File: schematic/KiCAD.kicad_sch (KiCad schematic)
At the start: 7 parts, among them J1 Raspberry_Pi_4, U1 NUCLEO-F401RE, U2 ACS712xLCTR-05B, U3 ACS712xLCTR-05B, U4 ACS712xLCTR-05B, U5 L298N

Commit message: new schematic
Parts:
- removed U6: (no value), Package_DFN_QFN:WDFN-10-1EP_3x3mm_P0.5mm_EP1.8x2.5mm, symbol Lab2_Modules:HW688_Buck
- added Buck-converter: (no value), symbol Lab2_Modules:HW688_Buck
- added Left-Rear-Motor, Right-Rear-Motor: (no value), symbol Lab2_Modules:Motor_With_Encoder
- added Servo: (no value), symbol Lab2_Modules:Servo
- U2: value ACS712xLCTR-05B -> Left Rear Motor Current sensor
- U3: value ACS712xLCTR-05B -> Right Rear Motor Current sensor
- U4: value ACS712xLCTR-05B -> Servo Current Sensor
- U5: value L298N -> H bridge
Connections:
- new net GND_S2: U1.10_20 (GND_S2), U1.10_9 (GND_S2)

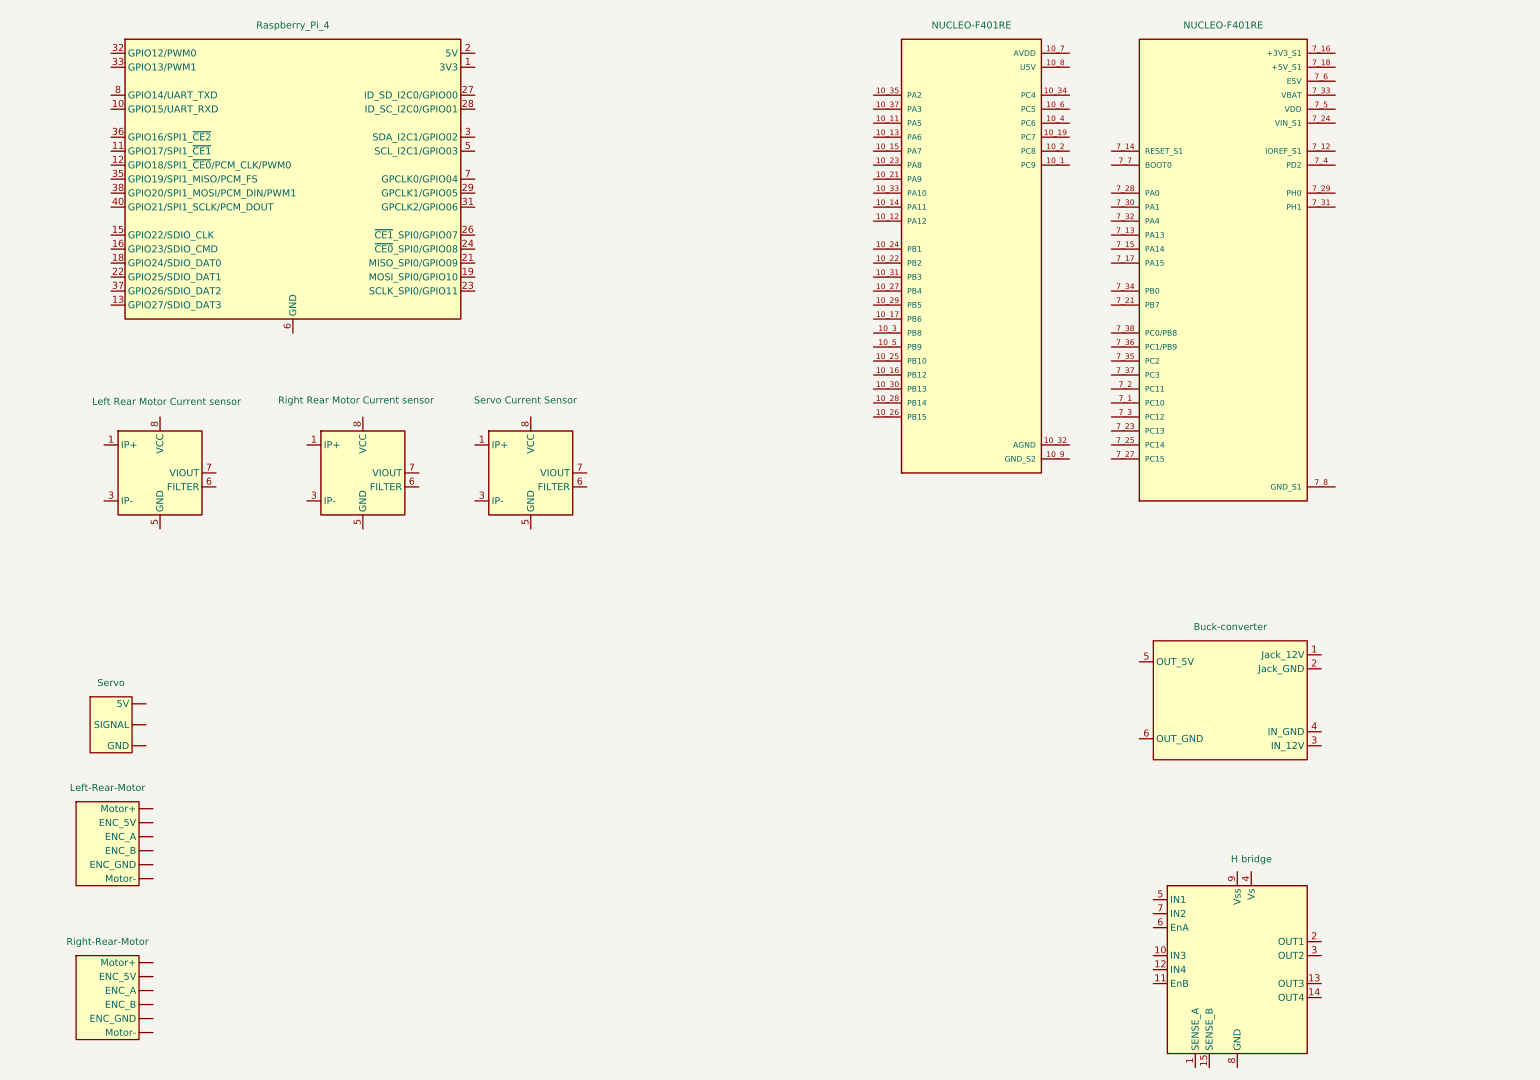
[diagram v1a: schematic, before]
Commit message: Updated schematic connections
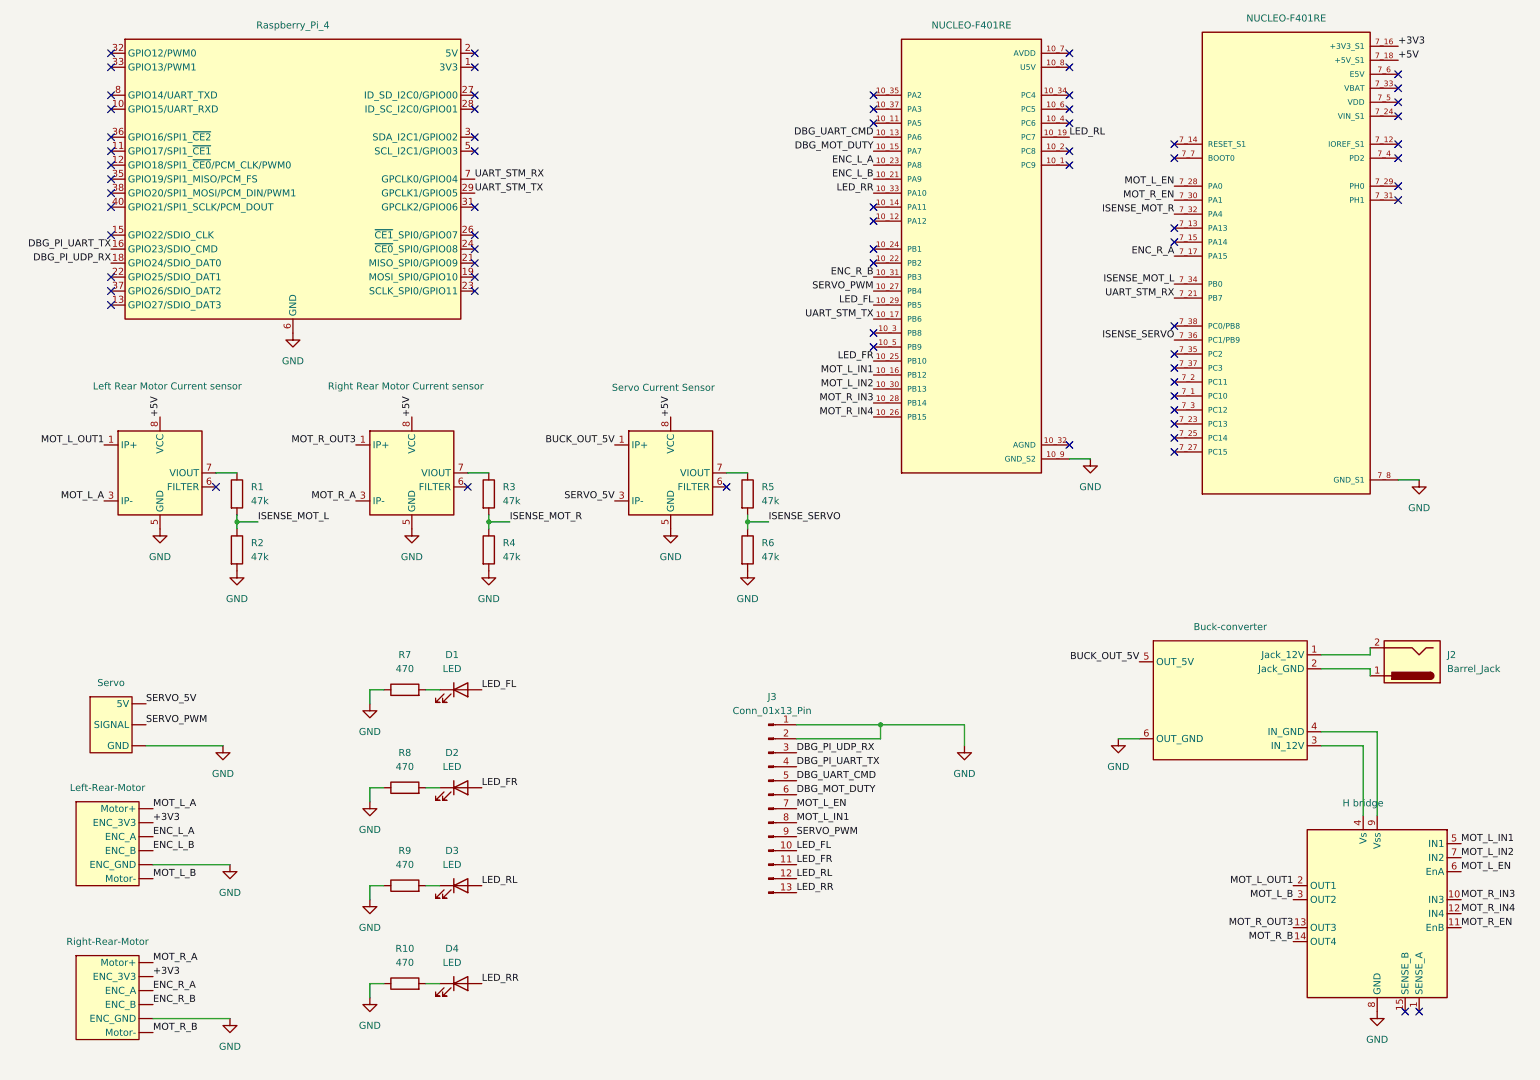
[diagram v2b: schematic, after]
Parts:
- added D1, D2, D3, D4: LED, symbol Device:LED
- added J2: Barrel_Jack, symbol Connector:Barrel_Jack
- added J3: Conn_01x13_Pin, symbol Connector:Conn_01x13_Pin
- added R1, R2, R3, R4, R5, R6: 47k, Diode_SMD:D_MiniMELF, symbol Device:R
- added R10, R7, R8, R9: 470, Diode_SMD:D_MiniMELF, symbol Device:R
- added unit 1 of U1
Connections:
- net GND_S2 is gone; now on net GND: U1.10_20 (GND_S2), U1.10_9 (GND_S2)
- net GND: now reaches J1.14 (GND), J1.20 (GND), J1.25 (GND), J1.30 (GND), J1.34 (GND), J1.39 (GND), J1.6 (GND), J1.9 (GND)
- net GND: now also Buck-converter.6 (OUT_GND), Left-Rear-Motor. (Motor-), Right-Rear-Motor. (Motor-), Servo. (GND), U2.5 (GND), U3.5 (GND), U4.5 (GND), U5.8 (GND), J3.1 (Pin_1), J3.2 (Pin_2), R10.1, R2.2, R4.2, R6.2, R7.1, R8.1, R9.1, U1.7_19 (GND_S1), U1.7_20 (GND_S1), U1.7_22 (GND_S1), U1.7_8 (GND_S1)
- net DBG_PI_UART_TX: now reaches J1.16 (GPIO23/SDIO_CMD)
- net DBG_PI_UART_TX: now also J3.4 (Pin_4)
- net DBG_PI_UDP_RX: now reaches J1.18 (GPIO24/SDIO_DAT0)
- net DBG_PI_UDP_RX: now also J3.3 (Pin_3)
- net UART_STM_TX: now reaches J1.29 (GPCLK1/GPIO05)
- net UART_STM_TX: now also U1.10_17 (PB6)
- net UART_STM_RX: now reaches J1.7 (GPCLK0/GPIO04)
- net UART_STM_RX: now also U1.7_21 (PB7)
- net MOT_R_IN3: now reaches U5.10 (IN3)
- net MOT_R_IN3: now also U1.10_28 (PB14)
- net MOT_R_EN: now reaches U5.11 (EnB)
- net MOT_R_EN: now also U1.7_30 (PA1)
- net MOT_R_IN4: now reaches U5.12 (IN4)
- net MOT_R_IN4: now also U1.10_26 (PB15)
- net MOT_R_OUT3: now reaches U5.13 (OUT3)
- net MOT_R_OUT3: now also U3.1 (IP+), U3.2 (IP+)
- net MOT_R_B: now reaches U5.14 (OUT4)
- net MOT_R_B: now also Right-Rear-Motor. (Motor-)
- net MOT_L_OUT1: now reaches U5.2 (OUT1)
- net MOT_L_OUT1: now also U2.1 (IP+), U2.2 (IP+)
- net MOT_L_B: now reaches U5.3 (OUT2)
- net MOT_L_B: now also Left-Rear-Motor. (Motor-)
- net at U5.4 (Vs): now also Buck-converter.3 (IN_12V)
- net MOT_L_IN1: now reaches U5.5 (IN1)
- net MOT_L_IN1: now also U1.10_16 (PB12), J3.8 (Pin_8)
- net MOT_L_EN: now reaches U5.6 (EnA)
- net MOT_L_EN: now also J3.7 (Pin_7), U1.7_28 (PA0)
- net MOT_L_IN2: now reaches U5.7 (IN2)
- net MOT_L_IN2: now also U1.10_30 (PB13)
- net at U5.9 (Vss): now also Buck-converter.4 (IN_GND)
- net BUCK_OUT_5V: now reaches U4.1 (IP+), U4.2 (IP+)
- net BUCK_OUT_5V: now also Buck-converter.5 (OUT_5V)
- net SERVO_5V: now reaches U4.3 (IP-), U4.4 (IP-)
- net SERVO_5V: now also Servo. (GND)
- net at U4.7 (VIOUT): now also R5.1
- net +5V: now reaches U4.8 (VCC)
- net +5V: now also U2.8 (VCC), U3.8 (VCC), U1.7_18 (+5V_S1)
- net MOT_R_A: now reaches U3.3 (IP-), U3.4 (IP-)
- net MOT_R_A: now also Right-Rear-Motor. (Motor-)
- net at U3.7 (VIOUT): now also R3.1
- net DBG_UART_CMD: now reaches U1.10_13 (PA6)
- net DBG_UART_CMD: now also J3.5 (Pin_5)
- net DBG_MOT_DUTY: now reaches U1.10_15 (PA7)
- net DBG_MOT_DUTY: now also J3.6 (Pin_6)
- net LED_RL: now reaches U1.10_19 (PC7)
- net LED_RL: now also D3.2 (A), J3.12 (Pin_12)
- net ENC_L_B: now reaches U1.10_21 (PA9)
- net ENC_L_B: now also Left-Rear-Motor. (Motor-)
- net ENC_L_A: now reaches U1.10_23 (PA8)
- net ENC_L_A: now also Left-Rear-Motor. (Motor-)
- net LED_FR: now reaches U1.10_25 (PB10)
- net LED_FR: now also D2.2 (A), J3.11 (Pin_11)
- net SERVO_PWM: now reaches U1.10_27 (PB4)
- net SERVO_PWM: now also Servo. (GND), J3.9 (Pin_9)
- net LED_FL: now reaches U1.10_29 (PB5)
- net LED_FL: now also D1.2 (A), J3.10 (Pin_10)
- net ENC_R_B: now reaches U1.10_31 (PB3)
- net ENC_R_B: now also Right-Rear-Motor. (Motor-)
- net LED_RR: now reaches U1.10_33 (PA10)
- net LED_RR: now also D4.2 (A), J3.13 (Pin_13)
- net at Buck-converter.1 (Jack_12V): now also J2.2
- net at Buck-converter.2 (Jack_GND): now also J2.1
- net MOT_L_A: now reaches U2.3 (IP-), U2.4 (IP-)
- net MOT_L_A: now also Left-Rear-Motor. (Motor-)
- net at U2.7 (VIOUT): now also R1.1
- removed net GND_S1: U1.7_19 (GND_S1), U1.7_20 (GND_S1), U1.7_22 (GND_S1), U1.7_8 (GND_S1)
- new net: D2.1 (K), R8.2
- new net: D1.1 (K), R7.2
- new net: D4.1 (K), R10.2
- new net: D3.1 (K), R9.2
- new net +3V3: Left-Rear-Motor. (Motor-), Right-Rear-Motor. (Motor-), U1.7_16 (+3V3_S1)
- new net ENC_R_A: Right-Rear-Motor. (Motor-), U1.7_17 (PA15)
- new net ISENSE_MOT_L: R1.2, R2.1, U1.7_34 (PB0)
- new net ISENSE_MOT_R: R3.2, R4.1, U1.7_32 (PA4)
- new net ISENSE_SERVO: R5.2, R6.1, U1.7_36 (PC1/PB9)
- no-connect marks 0 -> 69
